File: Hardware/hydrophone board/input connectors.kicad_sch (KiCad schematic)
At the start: 8 parts, among them J5 Conn_01x02, J6 Conn_01x02, J7 Conn_01x02, J8 Conn_01x02

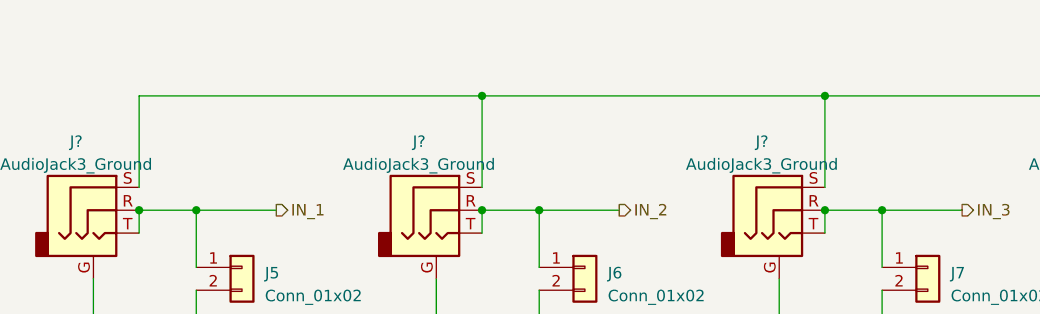
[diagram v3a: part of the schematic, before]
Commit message: assigned footprints
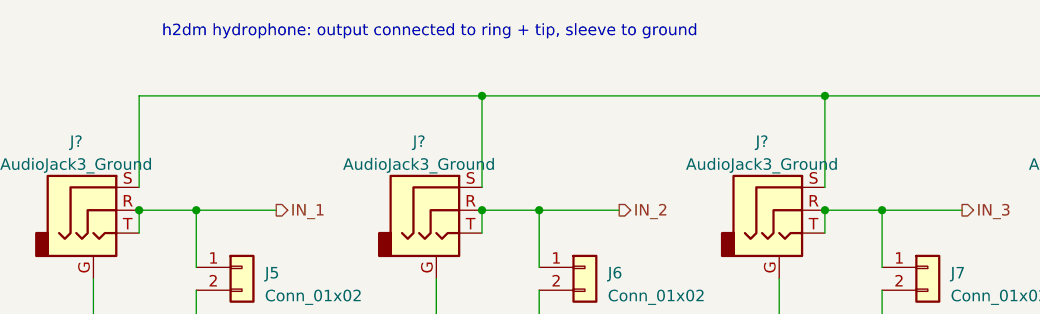
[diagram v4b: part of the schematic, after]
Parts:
- J5, J6, J7, J8: footprint (none) -> Connector_PinHeader_2.54mm:PinHeader_1x02_P2.54mm_Vertical
- J? (x4): footprint (none) -> Connector_Audio:Jack_3.5mm_CUI_SJ-3524-SMT_Horizontal
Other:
- note added: "h2dm hydrophone: output connected to ring + tip, sleeve to ground"
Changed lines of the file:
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@@
     (stroke (width 0) (type default))
   )
+  (text "h2dm hydrophone: output connected to ring + tip, sleeve to ground"
+    (at 63.5 50.8 0)
+    (effects (font (size 1.27 1.27)) (justify left bottom))
+  )
   (hierarchical_label "IN_2" (shape output) (at 114.3 69.85 0) (fields_autoplaced)
     (effects (font (size 1.27 1.27)) (justify left))
@@
       (effects (font (size 1.27 1.27)))
     )
-    (property "Footprint" "" (at 55.88 69.85 0)
+    (property "Footprint" "Connector_Audio:Jack_3.5mm_CUI_SJ-3524-SMT_Horizontal" (at 55.88 69.85 0)
       (effects (font (size 1.27 1.27)) hide)
     )
@@
       (effects (font (size 1.27 1.27)) (justify left))
     )
-    (property "Footprint" "" (at 110.49 76.2 0)
+    (property "Footprint" "Connector_PinHeader_2.54mm:PinHeader_1x02_P2.54mm_Vertical" (at 110.49 76.2 0)
       (effects (font (size 1.27 1.27)) hide)
     )
@@
       (effects (font (size 1.27 1.27)) (justify left))
     )
-    (property "Footprint" "" (at 72.39 76.2 0)
+    (property "Footprint" "Connector_PinHeader_2.54mm:PinHeader_1x02_P2.54mm_Vertical" (at 72.39 76.2 0)
       (effects (font (size 1.27 1.27)) hide)
     )
@@
       (effects (font (size 1.27 1.27)))
     )
-    (property "Footprint" "" (at 93.98 69.85 0)
+    (property "Footprint" "Connector_Audio:Jack_3.5mm_CUI_SJ-3524-SMT_Horizontal" (at 93.98 69.85 0)
       (effects (font (size 1.27 1.27)) hide)
     )
@@
       (effects (font (size 1.27 1.27)) (justify left))
     )
-    (property "Footprint" "" (at 148.59 76.2 0)
+    (property "Footprint" "Connector_PinHeader_2.54mm:PinHeader_1x02_P2.54mm_Vertical" (at 148.59 76.2 0)
       (effects (font (size 1.27 1.27)) hide)
     )
@@
       (effects (font (size 1.27 1.27)))
     )
-    (property "Footprint" "" (at 132.08 69.85 0)
+    (property "Footprint" "Connector_Audio:Jack_3.5mm_CUI_SJ-3524-SMT_Horizontal" (at 132.08 69.85 0)
       (effects (font (size 1.27 1.27)) hide)
     )
@@
       (effects (font (size 1.27 1.27)))
     )
-    (property "Footprint" "" (at 170.18 69.85 0)
+    (property "Footprint" "Connector_Audio:Jack_3.5mm_CUI_SJ-3524-SMT_Horizontal" (at 170.18 69.85 0)
       (effects (font (size 1.27 1.27)) hide)
     )
@@
       (effects (font (size 1.27 1.27)) (justify left))
     )
-    (property "Footprint" "" (at 186.69 76.2 0)
-      (effects (font (size 1.27 1.27)) hide)
-    )
+    (property "Footprint" "Connector_PinHeader_2.54mm:PinHeader_1x02_P2.54mm_Vertical" (at 186.69 76.2 0)
+      (effects (font (size 1.27 1.27)) hide)
+    )

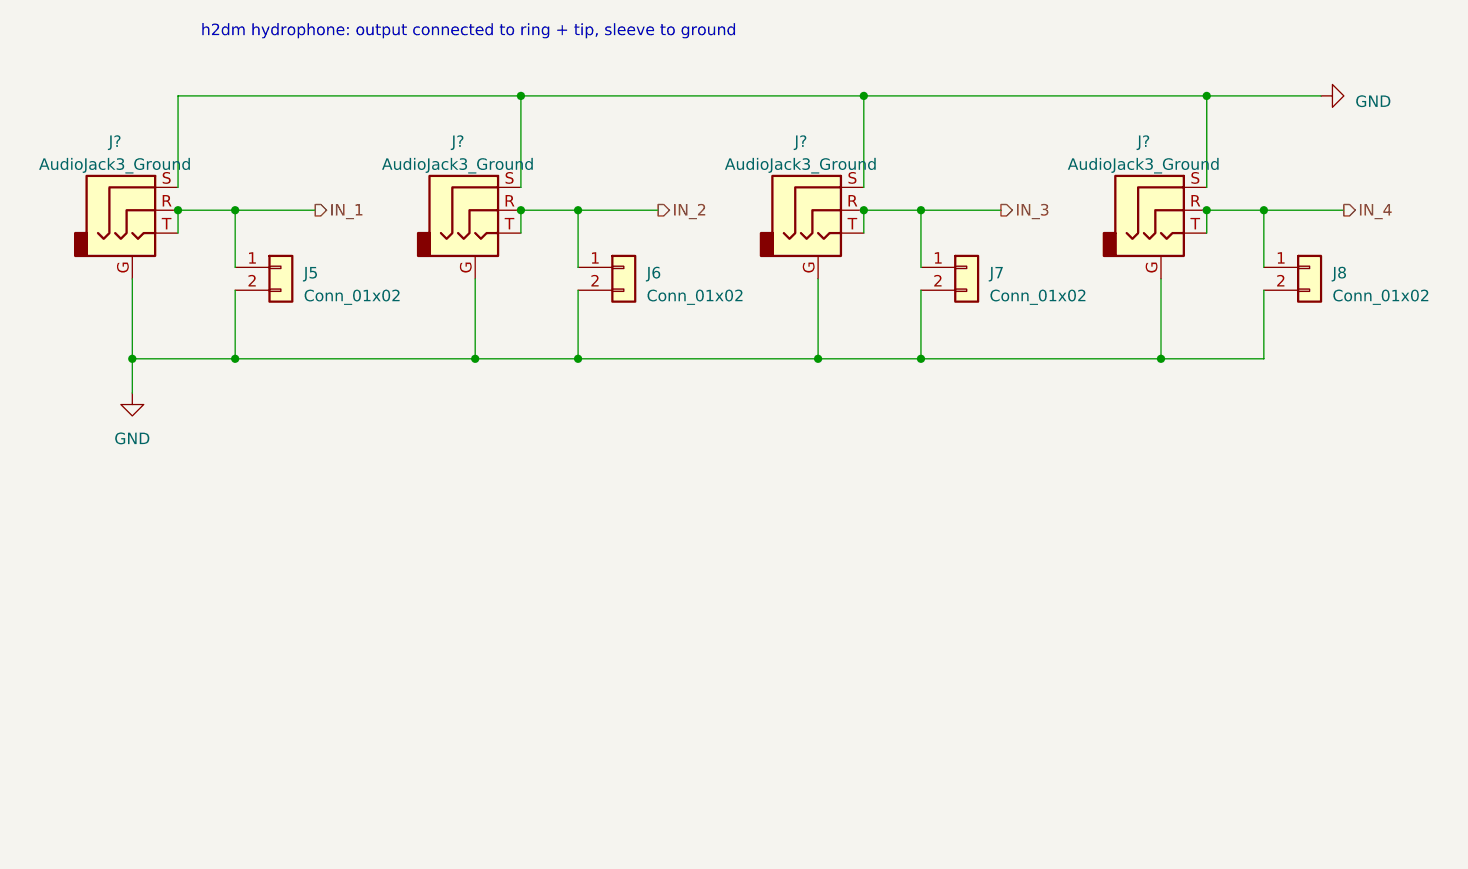
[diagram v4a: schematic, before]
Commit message: changed all cap + resistors to 0805, starting filter layout
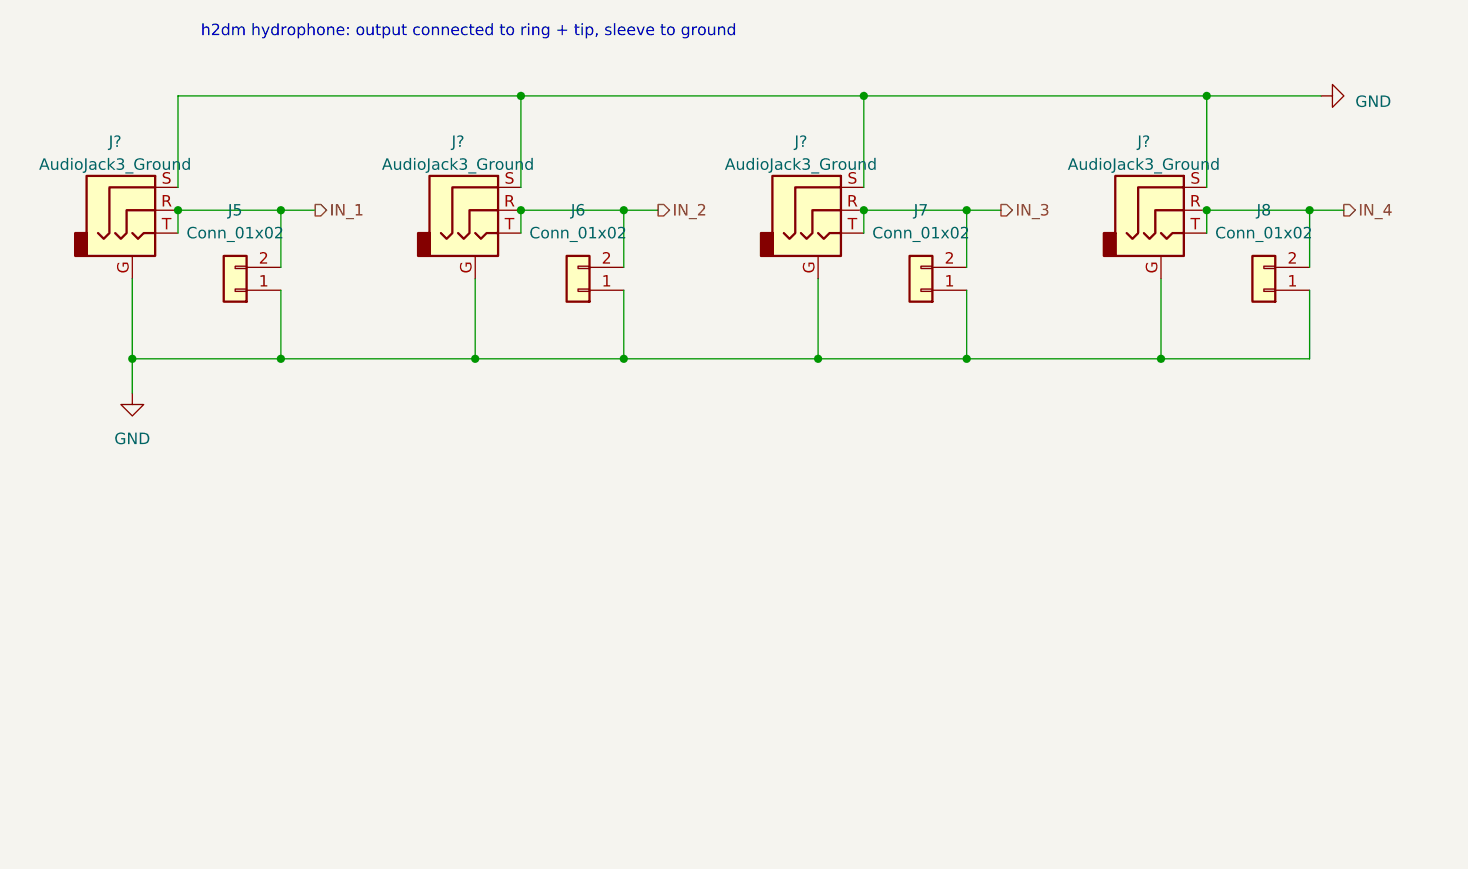
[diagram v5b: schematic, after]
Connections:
- net GND: now also J5.1 (Pin_1), J6.1 (Pin_1), J7.1 (Pin_1), J8.1 (Pin_1); no longer J5.2 (Pin_2), J6.2 (Pin_2), J7.2 (Pin_2), J8.2 (Pin_2)
- net IN_1: now also J5.2 (Pin_2); no longer J5.1 (Pin_1)
- net IN_2: now also J6.2 (Pin_2); no longer J6.1 (Pin_1)
- net IN_3: now also J7.2 (Pin_2); no longer J7.1 (Pin_1)
- net IN_4: now also J8.2 (Pin_2); no longer J8.1 (Pin_1)
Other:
- moved on the sheet: J5, J6, J7, J8

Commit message: changed audio jack footprint
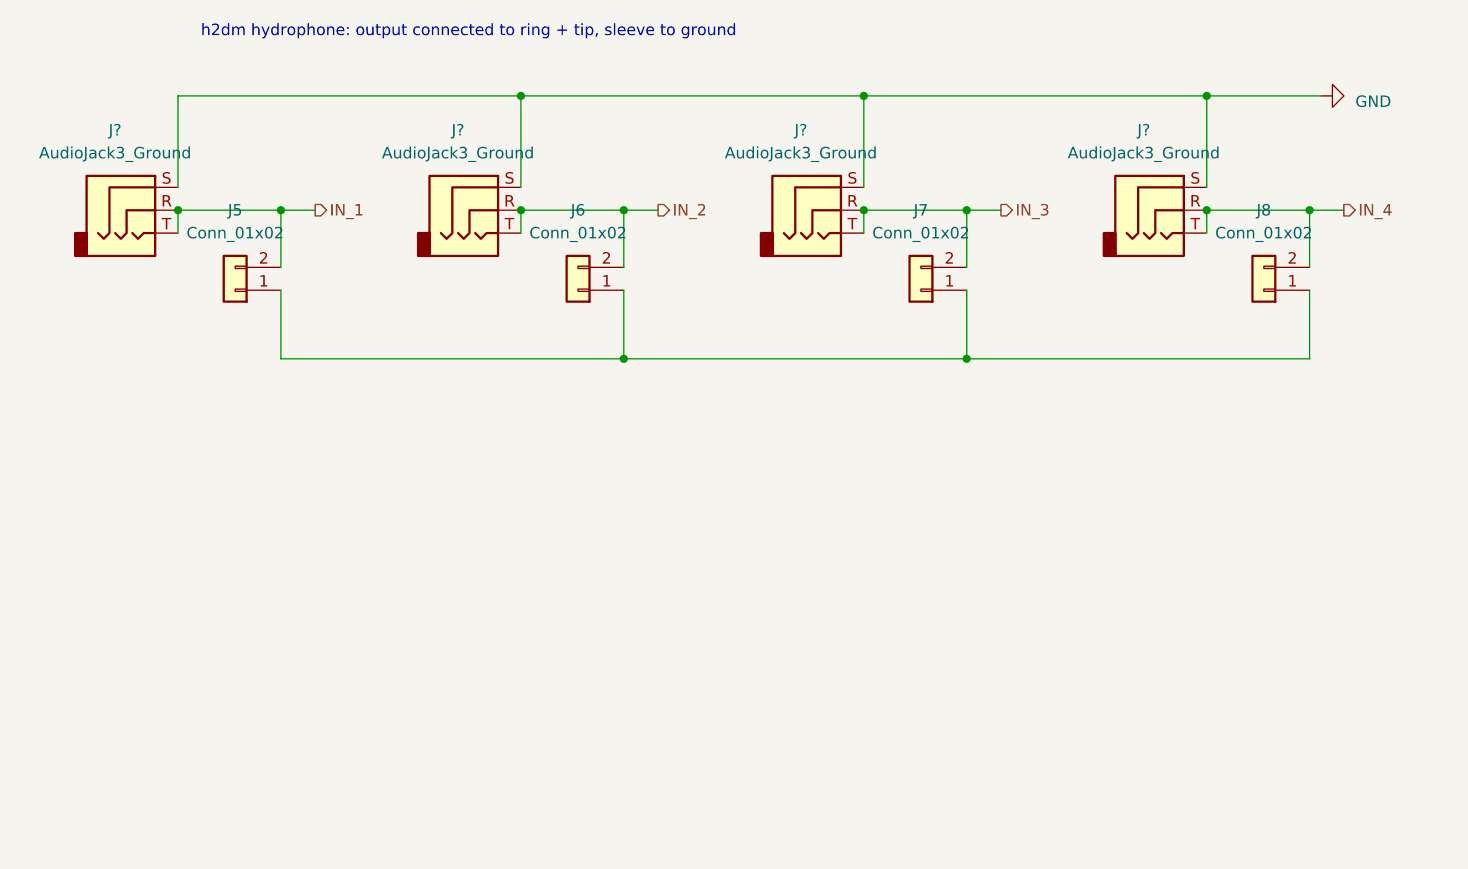
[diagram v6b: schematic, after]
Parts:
- J? (x4): footprint Connector_Audio:Jack_3.5mm_CUI_SJ-3524-SMT_Horizontal -> Connector_Audio:Jack_3.5mm_CUI_SJ-3523-SMT_Horizontal; symbol Connector_Audio:AudioJack3_Ground -> Connector_Audio:AudioJack3
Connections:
- net GND: no longer J5.1 (Pin_1), J6.1 (Pin_1), J7.1 (Pin_1), J8.1 (Pin_1), J?.G, J?.G, J?.G, J?.G
- new net: J5.1 (Pin_1), J6.1 (Pin_1), J7.1 (Pin_1), J8.1 (Pin_1)
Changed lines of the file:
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@@
 (kicad_sch (version 20230121) (generator eeschema)
   (paper "A4")
-  (junction (at 93.98 86.36) (diameter 0) (color 0 0 0 0)
-  )
-  (junction (at 55.88 86.36) (diameter 0) (color 0 0 0 0)
-  )
-  (junction (at 72.39 86.36) (diameter 0) (color 0 0 0 0)
-  )
   (junction (at 175.26 57.15) (diameter 0) (color 0 0 0 0)
   )
@@
   (junction (at 175.26 69.85) (diameter 0) (color 0 0 0 0)
   )
-  (junction (at 170.18 86.36) (diameter 0) (color 0 0 0 0)
-  )
   (junction (at 137.16 69.85) (diameter 0) (color 0 0 0 0)
   )
@@
   (junction (at 137.16 57.15) (diameter 0) (color 0 0 0 0)
   )
-  (junction (at 132.08 86.36) (diameter 0) (color 0 0 0 0)
-  )
   (junction (at 60.96 69.85) (diameter 0) (color 0 0 0 0)
   )
@@
   (junction (at 148.59 86.36) (diameter 0) (color 0 0 0 0)
   )
-  (wire (pts (xy 148.59 86.36) (xy 132.08 86.36))
+  (wire (pts (xy 110.49 86.36) (xy 148.59 86.36))
     (stroke (width 0) (type default))
   )
@@
     (stroke (width 0) (type default))
   )
-  (wire (pts (xy 110.49 86.36) (xy 93.98 86.36))
-    (stroke (width 0) (type default))
-  )
   (wire (pts (xy 72.39 78.74) (xy 72.39 86.36))
     (stroke (width 0) (type default))
   )
-  (wire (pts (xy 55.88 86.36) (xy 55.88 90.17))
-    (stroke (width 0) (type default))
-  )
-  (wire (pts (xy 170.18 77.47) (xy 170.18 86.36))
-    (stroke (width 0) (type default))
-  )
   (wire (pts (xy 60.96 69.85) (xy 72.39 69.85))
     (stroke (width 0) (type default))
@@
     (stroke (width 0) (type default))
   )
-  (wire (pts (xy 72.39 86.36) (xy 93.98 86.36))
+  (wire (pts (xy 72.39 86.36) (xy 110.49 86.36))
     (stroke (width 0) (type default))
   )
@@
     (stroke (width 0) (type default))
   )
-  (wire (pts (xy 170.18 86.36) (xy 148.59 86.36))
+  (wire (pts (xy 148.59 86.36) (xy 186.69 86.36))
     (stroke (width 0) (type default))
   )
@@
     (stroke (width 0) (type default))
   )
-  (wire (pts (xy 93.98 77.47) (xy 93.98 86.36))
-    (stroke (width 0) (type default))
-  )
-  (wire (pts (xy 132.08 77.47) (xy 132.08 86.36))
-    (stroke (width 0) (type default))
-  )
   (wire (pts (xy 99.06 57.15) (xy 99.06 67.31))
     (stroke (width 0) (type default))
@@
     (stroke (width 0) (type default))
   )
-  (wire (pts (xy 55.88 77.47) (xy 55.88 86.36))
-    (stroke (width 0) (type default))
-  )
-  (wire (pts (xy 132.08 86.36) (xy 110.49 86.36))
-    (stroke (width 0) (type default))
-  )
   (wire (pts (xy 72.39 69.85) (xy 72.39 76.2))
     (stroke (width 0) (type default))
@@
     (stroke (width 0) (type default))
   )
-  (wire (pts (xy 55.88 86.36) (xy 72.39 86.36))
-    (stroke (width 0) (type default))
-  )
   (wire (pts (xy 72.39 69.85) (xy 76.2 69.85))
     (stroke (width 0) (type default))
   )
   (wire (pts (xy 60.96 67.31) (xy 60.96 57.15))
-    (stroke (width 0) (type default))
-  )
-  (wire (pts (xy 186.69 86.36) (xy 170.18 86.36))
     (stroke (width 0) (type default))
   )
@@
     (effects (font (size 1.27 1.27)) (justify left))
   )
-  (symbol (lib_id "Connector_Audio:AudioJack3_Ground") (at 55.88 69.85 0) (unit 1)
-    (in_bom yes) (on_board yes) (dnp no) (fields_autoplaced)
-    (property "Reference" "J?" (at 53.975 62.23 0)
-      (effects (font (size 1.27 1.27)))
-    )
-    (property "Value" "AudioJack3_Ground" (at 53.975 64.77 0)
-      (effects (font (size 1.27 1.27)))
-    )
-    (property "Footprint" "Connector_Audio:Jack_3.5mm_CUI_SJ-3524-SMT_Horizontal" (at 55.88 69.85 0)
+  (symbol (lib_id "Connector_Audio:AudioJack3") (at 55.88 69.85 0) (unit 1)
+    (in_bom yes) (on_board yes) (dnp no) (fields_autoplaced)
+    (property "Reference" "J?" (at 53.975 60.96 0)
+      (effects (font (size 1.27 1.27)))
+    )
+    (property "Value" "AudioJack3_Ground" (at 53.975 63.5 0)
+      (effects (font (size 1.27 1.27)))
+    )
+    (property "Footprint" "Connector_Audio:Jack_3.5mm_CUI_SJ-3523-SMT_Horizontal" (at 55.88 69.85 0)
       (effects (font (size 1.27 1.27)) hide)
     )
@@
       (effects (font (size 1.27 1.27)) hide)
     )
-    (pin "G")
     (pin "R")
     (pin "S")
@@
     )
   )
-  (symbol (lib_id "Connector_Audio:AudioJack3_Ground") (at 93.98 69.85 0) (unit 1)
-    (in_bom yes) (on_board yes) (dnp no) (fields_autoplaced)
-    (property "Reference" "J?" (at 92.075 62.23 0)
-      (effects (font (size 1.27 1.27)))
-    )
-    (property "Value" "AudioJack3_Ground" (at 92.075 64.77 0)
-      (effects (font (size 1.27 1.27)))
-    )
-    (property "Footprint" "Connector_Audio:Jack_3.5mm_CUI_SJ-3524-SMT_Horizontal" (at 93.98 69.85 0)
+  (symbol (lib_id "Connector_Audio:AudioJack3") (at 93.98 69.85 0) (unit 1)
+    (in_bom yes) (on_board yes) (dnp no) (fields_autoplaced)
+    (property "Reference" "J?" (at 92.075 60.96 0)
+      (effects (font (size 1.27 1.27)))
+    )
+    (property "Value" "AudioJack3_Ground" (at 92.075 63.5 0)
+      (effects (font (size 1.27 1.27)))
+    )
+    (property "Footprint" "Connector_Audio:Jack_3.5mm_CUI_SJ-3523-SMT_Horizontal" (at 93.98 69.85 0)
       (effects (font (size 1.27 1.27)) hide)
     )
@@
       (effects (font (size 1.27 1.27)) hide)
     )
-    (pin "G")
     (pin "R")
     (pin "S")
@@
     )
   )
-  (symbol (lib_id "Connector_Audio:AudioJack3_Ground") (at 132.08 69.85 0) (unit 1)
-    (in_bom yes) (on_board yes) (dnp no) (fields_autoplaced)
-    (property "Reference" "J?" (at 130.175 62.23 0)
-      (effects (font (size 1.27 1.27)))
-    )
-    (property "Value" "AudioJack3_Ground" (at 130.175 64.77 0)
-      (effects (font (size 1.27 1.27)))
-    )
-    (property "Footprint" "Connector_Audio:Jack_3.5mm_CUI_SJ-3524-SMT_Horizontal" (at 132.08 69.85 0)
+  (symbol (lib_id "Connector_Audio:AudioJack3") (at 132.08 69.85 0) (unit 1)
+    (in_bom yes) (on_board yes) (dnp no) (fields_autoplaced)
+    (property "Reference" "J?" (at 130.175 60.96 0)
+      (effects (font (size 1.27 1.27)))
+    )
+    (property "Value" "AudioJack3_Ground" (at 130.175 63.5 0)
+      (effects (font (size 1.27 1.27)))
+    )
+    (property "Footprint" "Connector_Audio:Jack_3.5mm_CUI_SJ-3523-SMT_Horizontal" (at 132.08 69.85 0)
       (effects (font (size 1.27 1.27)) hide)
     )
@@
       (effects (font (size 1.27 1.27)) hide)
     )
-    (pin "G")
     (pin "R")
     (pin "S")
@@
     )
   )
-  (symbol (lib_id "Connector_Audio:AudioJack3_Ground") (at 170.18 69.85 0) (unit 1)
-    (in_bom yes) (on_board yes) (dnp no) (fields_autoplaced)
-    (property "Reference" "J?" (at 168.275 62.23 0)
-      (effects (font (size 1.27 1.27)))
-    )
-    (property "Value" "AudioJack3_Ground" (at 168.275 64.77 0)
-      (effects (font (size 1.27 1.27)))
-    )
-    (property "Footprint" "Connector_Audio:Jack_3.5mm_CUI_SJ-3524-SMT_Horizontal" (at 170.18 69.85 0)
+  (symbol (lib_id "Connector_Audio:AudioJack3") (at 170.18 69.85 0) (unit 1)
+    (in_bom yes) (on_board yes) (dnp no) (fields_autoplaced)
+    (property "Reference" "J?" (at 168.275 60.96 0)
+      (effects (font (size 1.27 1.27)))
+    )
+    (property "Value" "AudioJack3_Ground" (at 168.275 63.5 0)
+      (effects (font (size 1.27 1.27)))
+    )
+    (property "Footprint" "Connector_Audio:Jack_3.5mm_CUI_SJ-3523-SMT_Horizontal" (at 170.18 69.85 0)
       (effects (font (size 1.27 1.27)) hide)
     )
@@
       (effects (font (size 1.27 1.27)) hide)
     )
-    (pin "G")
     (pin "R")
     (pin "S")
@@
         )
       )
-    )
-  )
-  (symbol (lib_id "power:GND") (at 55.88 90.17 0) (unit 1)
-    (in_bom yes) (on_board yes) (dnp no) (fields_autoplaced)
-    (property "Reference" "#PWR02" (at 55.88 96.52 0)
-      (effects (font (size 1.27 1.27)) hide)
-    )
-    (property "Value" "GND" (at 55.88 95.25 0)
-      (effects (font (size 1.27 1.27)))
-    )
-    (property "Footprint" "" (at 55.88 90.17 0)
-      (effects (font (size 1.27 1.27)) hide)
-    )
-    (property "Datasheet" "" (at 55.88 90.17 0)
-      (effects (font (size 1.27 1.27)) hide)
-    )
-    (pin "1")
-    (instances
-      (project "hydrophone board"
-        (path "/4356d3a6-6a00-447d-897e-473f60221539/1cfbaf71-7039-4355-8fc7-d8c77f0e8058"
-          (reference "#PWR02") (unit 1)
-        )
-      )
